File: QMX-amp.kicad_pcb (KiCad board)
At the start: 2 copper layers, 56.6 x 57.7 mm, 4 parts

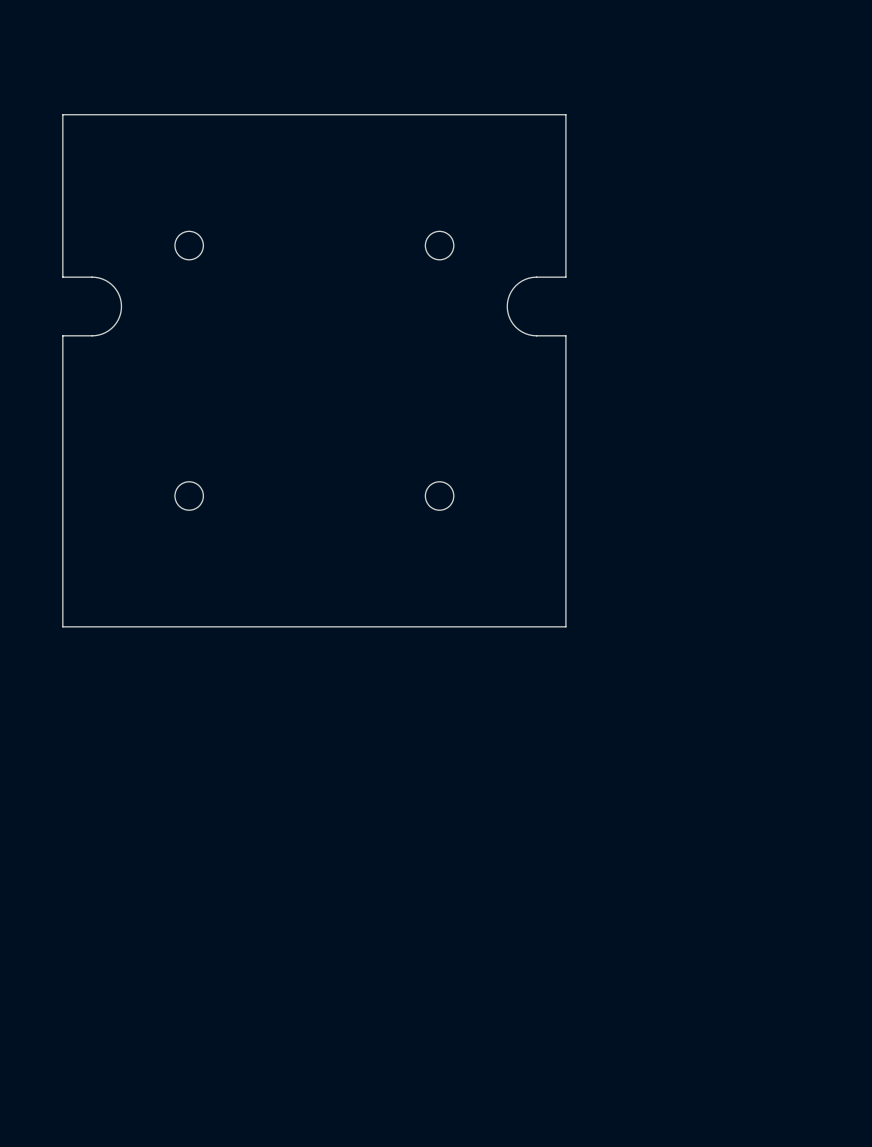
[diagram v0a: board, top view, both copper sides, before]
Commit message: PCB template now fits the QMX dead space
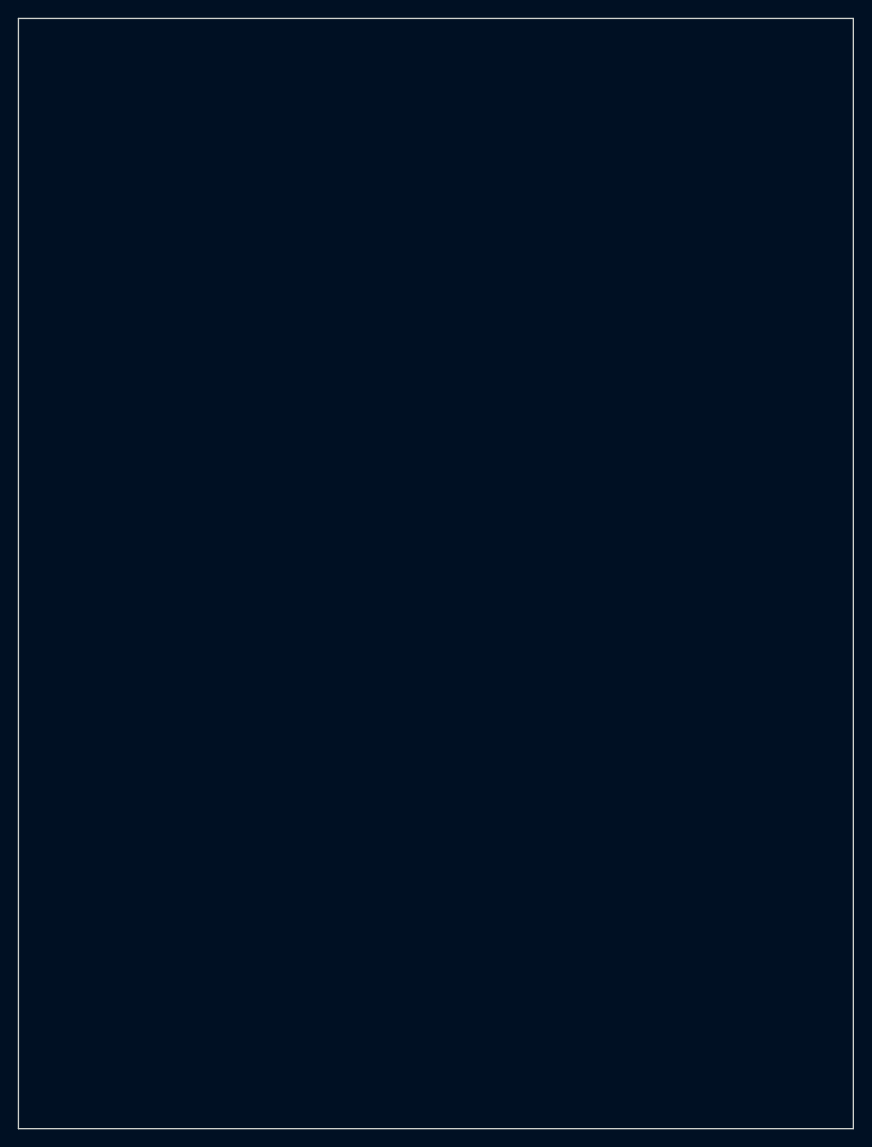
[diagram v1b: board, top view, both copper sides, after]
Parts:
- removed MH1, MH2, MH3, MH4: MountingHole_3.2mm_M3_ISO7380, MountingHole:MountingHole_3.2mm_M3_ISO7380
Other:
- board size 56.6 x 57.7 mm -> 94 x 125 mm

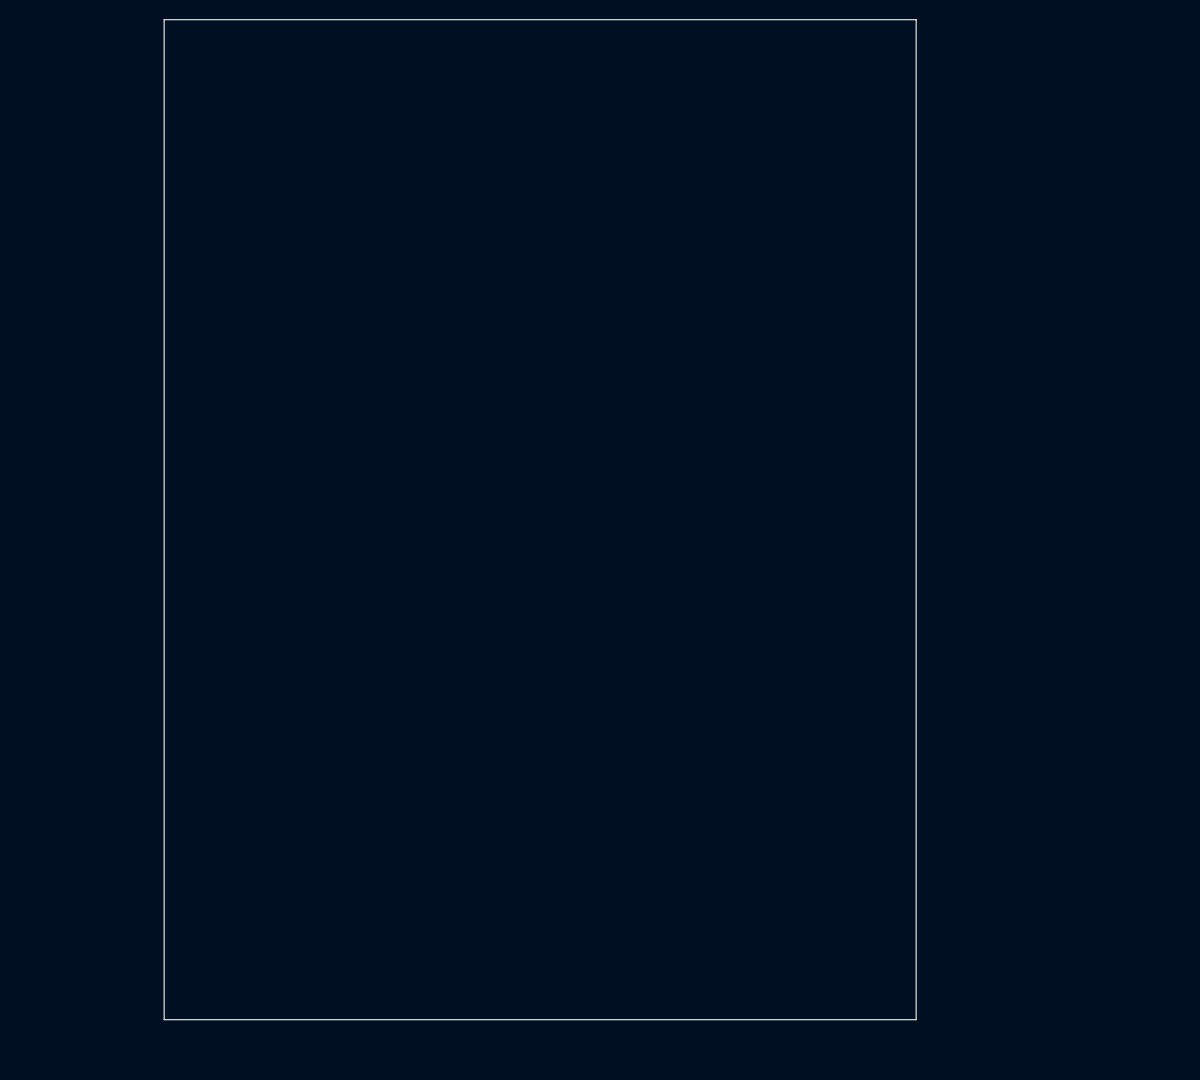
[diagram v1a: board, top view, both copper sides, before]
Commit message: v0.9 ERC passes.  All parts have footprints.  Need to renumber pages so things related are closer in printout
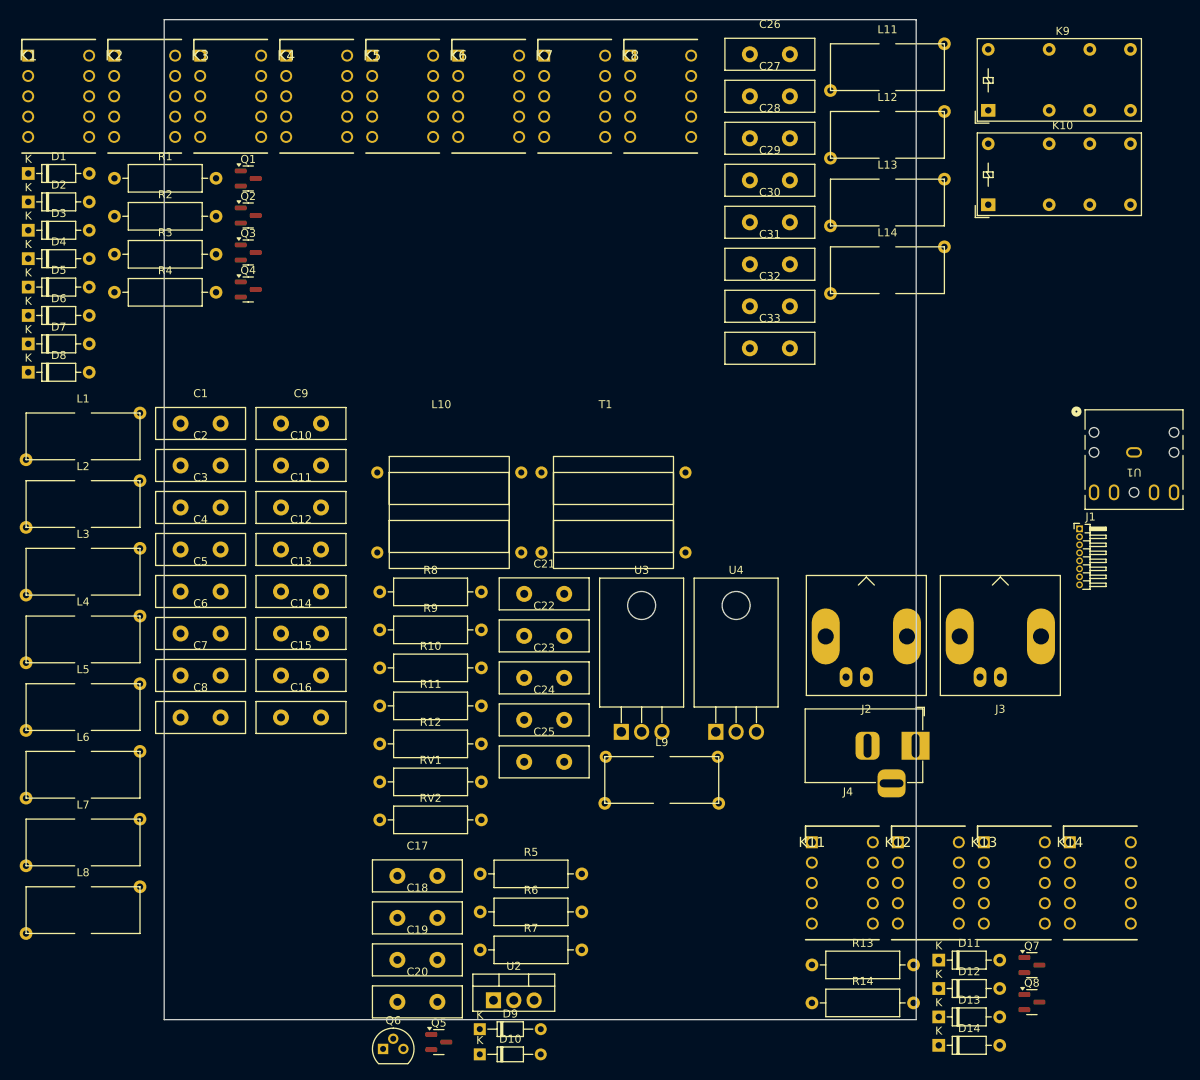
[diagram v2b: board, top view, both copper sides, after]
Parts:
- added C1: 1200 pF, ZZZMyLibrary:C_Disc_D11.0mm_W4.0mm_P5.00mm, F.Cu at (97.0, 82.0)
- added C10: 100 pF, ZZZMyLibrary:C_Disc_D11.0mm_W4.0mm_P5.00mm, F.Cu at (109.6, 87.2)
- added C11: 47 pF, ZZZMyLibrary:C_Disc_D11.0mm_W4.0mm_P5.00mm, F.Cu at (109.6, 92.5)
- added C12: 36 pF, ZZZMyLibrary:C_Disc_D11.0mm_W4.0mm_P5.00mm, F.Cu at (109.6, 97.7)
- added C13: 820 pF, ZZZMyLibrary:C_Disc_D11.0mm_W4.0mm_P5.00mm, F.Cu at (109.6, 103.0)
- added C14: 660 pF, ZZZMyLibrary:C_Disc_D11.0mm_W4.0mm_P5.00mm, F.Cu at (109.6, 108.2)
- added C15: 360 pF, ZZZMyLibrary:C_Disc_D11.0mm_W4.0mm_P5.00mm, F.Cu at (109.6, 113.5)
- added C16: 180 pF, ZZZMyLibrary:C_Disc_D11.0mm_W4.0mm_P5.00mm, F.Cu at (109.6, 118.7)
- added C17: ? uF, ZZZMyLibrary:C_Disc_D11.0mm_W4.0mm_P5.00mm, F.Cu at (124.2, 138.5)
- added C18: 0.1 uF, ZZZMyLibrary:C_Disc_D11.0mm_W4.0mm_P5.00mm, F.Cu at (124.2, 143.8)
- added C19: 0.1 uF, ZZZMyLibrary:C_Disc_D11.0mm_W4.0mm_P5.00mm, F.Cu at (124.2, 149.0)
- added C2: 660 pF, ZZZMyLibrary:C_Disc_D11.0mm_W4.0mm_P5.00mm, F.Cu at (97.0, 87.2)
- added C20: 0.1 uF, ZZZMyLibrary:C_Disc_D11.0mm_W4.0mm_P5.00mm, F.Cu at (124.2, 154.3)
- added C21: 0.1, ZZZMyLibrary:C_Disc_D11.0mm_W4.0mm_P5.00mm, F.Cu at (140.0, 103.3)
- added C22: 0.01, ZZZMyLibrary:C_Disc_D11.0mm_W4.0mm_P5.00mm, F.Cu at (140.0, 108.5)
- added C23: 0.01, ZZZMyLibrary:C_Disc_D11.0mm_W4.0mm_P5.00mm, F.Cu at (140.0, 113.8)
- added C24: 0.1, ZZZMyLibrary:C_Disc_D11.0mm_W4.0mm_P5.00mm, F.Cu at (140.0, 119.0)
- added C25: 1 uF, ZZZMyLibrary:C_Disc_D11.0mm_W4.0mm_P5.00mm, F.Cu at (140.0, 124.3)
- added C26: 120 pF, ZZZMyLibrary:C_Disc_D11.0mm_W4.0mm_P5.00mm, F.Cu at (168.2, 35.8)
- added C27: 68 pF, ZZZMyLibrary:C_Disc_D11.0mm_W4.0mm_P5.00mm, F.Cu at (168.2, 41.1)
- added C28: 180 pF, ZZZMyLibrary:C_Disc_D11.0mm_W4.0mm_P5.00mm, F.Cu at (168.2, 46.3)
- added C29: 120 pF, ZZZMyLibrary:C_Disc_D11.0mm_W4.0mm_P5.00mm, F.Cu at (168.2, 51.6)
- added C3: 360 pF, ZZZMyLibrary:C_Disc_D11.0mm_W4.0mm_P5.00mm, F.Cu at (97.0, 92.5)
- added C30: 13 pF, ZZZMyLibrary:C_Disc_D11.0mm_W4.0mm_P5.00mm, F.Cu at (168.2, 56.8)
- added C31: 100 pF, ZZZMyLibrary:C_Disc_D11.0mm_W4.0mm_P5.00mm, F.Cu at (168.2, 62.1)
- added C32: 82 pF, ZZZMyLibrary:C_Disc_D11.0mm_W4.0mm_P5.00mm, F.Cu at (168.2, 67.3)
- added C33: 68 pF, ZZZMyLibrary:C_Disc_D11.0mm_W4.0mm_P5.00mm, F.Cu at (168.2, 72.6)
- added C4: 180 pF, ZZZMyLibrary:C_Disc_D11.0mm_W4.0mm_P5.00mm, F.Cu at (97.0, 97.7)
- added C5: 2200 pF, ZZZMyLibrary:C_Disc_D11.0mm_W4.0mm_P5.00mm, F.Cu at (97.0, 103.0)
- added C6: 1240 pF, ZZZMyLibrary:C_Disc_D11.0mm_W4.0mm_P5.00mm, F.Cu at (97.0, 108.2)
- added C7: 650 pF, ZZZMyLibrary:C_Disc_D11.0mm_W4.0mm_P5.00mm, F.Cu at (97.0, 113.5)
- added C8: 330 pF, ZZZMyLibrary:C_Disc_D11.0mm_W4.0mm_P5.00mm, F.Cu at (97.0, 118.7)
- added C9: 220 pF, ZZZMyLibrary:C_Disc_D11.0mm_W4.0mm_P5.00mm, F.Cu at (109.6, 82.0)
- added D1: 1N4148, Diode_THT:D_DO-35_SOD27_P7.62mm_Horizontal, F.Cu at (78.0, 50.7)
- added D10: 1N4148, Diode_THT:D_DO-34_SOD68_P7.62mm_Horizontal, F.Cu at (134.4, 160.8)
- added D11: 1N4148, Diode_THT:D_DO-35_SOD27_P7.62mm_Horizontal, F.Cu at (191.8, 149.1)
- added D12: 1N4148, Diode_THT:D_DO-35_SOD27_P7.62mm_Horizontal, F.Cu at (191.8, 152.6)
- added D13: 1N4148, Diode_THT:D_DO-35_SOD27_P7.62mm_Horizontal, F.Cu at (191.8, 156.2)
- added D14: 1N4148, Diode_THT:D_DO-35_SOD27_P7.62mm_Horizontal, F.Cu at (191.8, 159.7)
- added D2: 1N4148, Diode_THT:D_DO-35_SOD27_P7.62mm_Horizontal, F.Cu at (78.0, 54.3)
- added D3: 1N4148, Diode_THT:D_DO-35_SOD27_P7.62mm_Horizontal, F.Cu at (78.0, 57.8)
- added D4: 1N4148, Diode_THT:D_DO-35_SOD27_P7.62mm_Horizontal, F.Cu at (78.0, 61.4)
- added D5: 1N4148, Diode_THT:D_DO-35_SOD27_P7.62mm_Horizontal, F.Cu at (78.0, 64.9)
- added D6: 1N4148, Diode_THT:D_DO-35_SOD27_P7.62mm_Horizontal, F.Cu at (78.0, 68.5)
- added D7: 1N4148, Diode_THT:D_DO-35_SOD27_P7.62mm_Horizontal, F.Cu at (78.0, 72.0)
- added D8: 1N4148, Diode_THT:D_DO-35_SOD27_P7.62mm_Horizontal, F.Cu at (78.0, 75.6)
- added D9: 1N4148, Diode_THT:D_DO-34_SOD68_P7.62mm_Horizontal, F.Cu at (134.4, 157.7)
- added J1: Conn_01x08_Pin, Connector_PinHeader_1.00mm:PinHeader_1x08_P1.00mm_Horizontal, F.Cu at (209.4, 95.2)
- added J2: RF-IN, Connector_Coaxial:BNC_Amphenol_B6252HB-NPP3G-50_Horizontal, F.Cu at (182.8, 113.7)
- added J3: RF-OUT, Connector_Coaxial:BNC_Amphenol_B6252HB-NPP3G-50_Horizontal, F.Cu at (199.5, 113.7)
- added J4: Barrel_Jack_Switch, Connector_BarrelJack:BarrelJack_Horizontal, F.Cu at (188.9, 122.3)
- added K1: EA2-5NU, ZZZMyLibrary:DIPS762W70P254L1420H540Q10N, F.Cu at (78.0, 36.0)
- added K10: HK19F-DCxxV-SHC, Relay_THT:Relay_DPDT_Finder_30.22, F.Cu at (198.0, 54.6)
- added K11: EA2-5NU, ZZZMyLibrary:DIPS762W70P254L1420H540Q10N, F.Cu at (176.0, 134.3)
- added K12: EA2-5NU, ZZZMyLibrary:DIPS762W70P254L1420H540Q10N, F.Cu at (186.7, 134.3)
- added K13: EA2-5NU, ZZZMyLibrary:DIPS762W70P254L1420H540Q10N, F.Cu at (197.5, 134.3)
- added K14: EA2-5NU, ZZZMyLibrary:DIPS762W70P254L1420H540Q10N, F.Cu at (208.2, 134.3)
- added K2: EA2-5NU, ZZZMyLibrary:DIPS762W70P254L1420H540Q10N, F.Cu at (88.8, 36.0)
- added K3: EA2-5NU, ZZZMyLibrary:DIPS762W70P254L1420H540Q10N, F.Cu at (99.5, 36.0)
- added K4: EA2-5NU, ZZZMyLibrary:DIPS762W70P254L1420H540Q10N, F.Cu at (110.2, 36.0)
- added K5: EA2-5NU, ZZZMyLibrary:DIPS762W70P254L1420H540Q10N, F.Cu at (121.0, 36.0)
- added K6: EA2-5NU, ZZZMyLibrary:DIPS762W70P254L1420H540Q10N, F.Cu at (131.8, 36.0)
- added K7: EA2-5NU, ZZZMyLibrary:DIPS762W70P254L1420H540Q10N, F.Cu at (142.5, 36.0)
- added K8: EA2-5NU, ZZZMyLibrary:DIPS762W70P254L1420H540Q10N, F.Cu at (153.2, 36.0)
- added K9: HK19F-DCxxV-SHC, Relay_THT:Relay_DPDT_Finder_30.22, F.Cu at (198.0, 42.8)
- added L1: L, ZZZMyLibrary:Toroid_T50_Vertical_L14.0mm_W5.6mm, F.Cu at (84.9, 80.9)
- added L10: BN-43-7051, ZZZMyLibrary:BN-43-202-FLAT, F.Cu at (129.6, 80.1)
- added L11: L, ZZZMyLibrary:Toroid_T50_Vertical_L14.0mm_W5.6mm, F.Cu at (185.4, 34.8)
- added L12: L, ZZZMyLibrary:Toroid_T50_Vertical_L14.0mm_W5.6mm, F.Cu at (185.4, 43.2)
- added L13: L, ZZZMyLibrary:Toroid_T50_Vertical_L14.0mm_W5.6mm, F.Cu at (185.4, 51.7)
- added L14: L, ZZZMyLibrary:Toroid_T50_Vertical_L14.0mm_W5.6mm, F.Cu at (185.4, 60.2)
- added L2: L, ZZZMyLibrary:Toroid_T50_Vertical_L14.0mm_W5.6mm, F.Cu at (84.9, 89.4)
- added L3: L, ZZZMyLibrary:Toroid_T50_Vertical_L14.0mm_W5.6mm, F.Cu at (84.9, 97.9)
- added L4: L, ZZZMyLibrary:Toroid_T50_Vertical_L14.0mm_W5.6mm, F.Cu at (84.9, 106.3)
- added L5: L, ZZZMyLibrary:Toroid_T50_Vertical_L14.0mm_W5.6mm, F.Cu at (84.9, 114.8)
- added L6: L, ZZZMyLibrary:Toroid_T50_Vertical_L14.0mm_W5.6mm, F.Cu at (84.9, 123.2)
- added L7: L, ZZZMyLibrary:Toroid_T50_Vertical_L14.0mm_W5.6mm, F.Cu at (84.9, 131.7)
- added L8: L, ZZZMyLibrary:Toroid_T50_Vertical_L14.0mm_W5.6mm, F.Cu at (84.9, 140.2)
- added L9: FT50-43, ZZZMyLibrary:Toroid_T50_Vertical_L14.0mm_W5.6mm_4pins, F.Cu at (157.2, 123.9)
- added Q1: BSS123, Package_TO_SOT_SMD:SOT-23, F.Cu at (105.5, 51.4)
- added Q2: BSS123, Package_TO_SOT_SMD:SOT-23, F.Cu at (105.5, 56.0)
- added Q3: BSS123, Package_TO_SOT_SMD:SOT-23, F.Cu at (105.5, 60.6)
- added Q4: BSS123, Package_TO_SOT_SMD:SOT-23, F.Cu at (105.5, 65.2)
- added Q5: BSS123, Package_TO_SOT_SMD:SOT-23, F.Cu at (129.3, 159.3)
- added Q6: MPS-751, Package_TO_SOT_THT:TO-92, F.Cu at (122.4, 160.2)
- added Q7: BSS123, Package_TO_SOT_SMD:SOT-23, F.Cu at (203.5, 149.7)
- added Q8: BSS123, Package_TO_SOT_SMD:SOT-23, F.Cu at (203.5, 154.3)
- added R1: 47K, Resistor_THT:R_Axial_DIN0309_L9.0mm_D3.2mm_P12.70mm_Horizontal, F.Cu at (88.8, 51.3)
- added R10: 270, Resistor_THT:R_Axial_DIN0309_L9.0mm_D3.2mm_P12.70mm_Horizontal, F.Cu at (122.0, 112.5)
- added R11: 470, Resistor_THT:R_Axial_DIN0309_L9.0mm_D3.2mm_P12.70mm_Horizontal, F.Cu at (122.0, 117.3)
- added R12: 470, Resistor_THT:R_Axial_DIN0309_L9.0mm_D3.2mm_P12.70mm_Horizontal, F.Cu at (122.0, 122.0)
- added R13: 47K, Resistor_THT:R_Axial_DIN0309_L9.0mm_D3.2mm_P12.70mm_Horizontal, F.Cu at (176.0, 149.7)
- added R14: 47K, Resistor_THT:R_Axial_DIN0309_L9.0mm_D3.2mm_P12.70mm_Horizontal, F.Cu at (176.0, 154.4)
- added R2: 47K, Resistor_THT:R_Axial_DIN0309_L9.0mm_D3.2mm_P12.70mm_Horizontal, F.Cu at (88.8, 56.1)
- added R3: 47K, Resistor_THT:R_Axial_DIN0309_L9.0mm_D3.2mm_P12.70mm_Horizontal, F.Cu at (88.8, 60.8)
- added R4: 47K, Resistor_THT:R_Axial_DIN0309_L9.0mm_D3.2mm_P12.70mm_Horizontal, F.Cu at (88.8, 65.6)
- added R5: 47K, Resistor_THT:R_Axial_DIN0309_L9.0mm_D3.2mm_P12.70mm_Horizontal, F.Cu at (134.5, 138.3)
- added R6: 4.7K, Resistor_THT:R_Axial_DIN0309_L9.0mm_D3.2mm_P12.70mm_Horizontal, F.Cu at (134.5, 143.0)
- added R7: 4.7K, Resistor_THT:R_Axial_DIN0309_L9.0mm_D3.2mm_P12.70mm_Horizontal, F.Cu at (134.5, 147.8)
- added R8: 270, Resistor_THT:R_Axial_DIN0309_L9.0mm_D3.2mm_P12.70mm_Horizontal, F.Cu at (122.0, 103.0)
- added R9: 21, Resistor_THT:R_Axial_DIN0309_L9.0mm_D3.2mm_P12.70mm_Horizontal, F.Cu at (122.0, 107.8)
- added RV1: 20K, Resistor_THT:R_Axial_DIN0309_L9.0mm_D3.2mm_P12.70mm_Horizontal, F.Cu at (122.0, 126.8)
- added RV2: 20K, Resistor_THT:R_Axial_DIN0309_L9.0mm_D3.2mm_P12.70mm_Horizontal, F.Cu at (122.0, 131.5)
- added T1: BN-43-202, ZZZMyLibrary:BN-43-202-FLAT, F.Cu at (150.2, 80.1)
- added U1: SJ1-3523N, ZZZMyLibrary:SJ1-3523N_CUD, F.Cu at (211.2, 82.6)
- added U2: LM7805_TO220, Package_TO_SOT_THT:TO-220-3_Vertical, F.Cu at (136.2, 154.1)
- added U3: RD16HHF1, Package_TO_SOT_THT:TO-220F-3_Horizontal_TabDown, F.Cu at (152.1, 120.5)
- added U4: RD16HHF1, Package_TO_SOT_THT:TO-220F-3_Horizontal_TabDown, F.Cu at (163.9, 120.5)

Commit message: checkpoint before I shrink width of capps  so things might fit PCB
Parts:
- RV1, RV2: footprint Resistor_THT:R_Axial_DIN0309_L9.0mm_D3.2mm_P12.70mm_Horizontal -> Potentiometer_THT:Potentiometer_Piher_PT-10-V05_Vertical
- moved U3 161.3 mm to (-8.74, 132.1)
- moved U4 161.3 mm to (3.07, 132.1)
- moved L9 138.9 mm to (20.0, 101.9)
- moved C17 132.5 mm to (-8.33, 139.7)
- moved C18 132.5 mm to (-8.33, 144.9)
- moved C19 132.5 mm to (-8.33, 150.2)
- moved C20 132.5 mm to (-8.33, 155.4)
- moved Q5 132.5 mm to (-3.15, 160.5)
- moved D10 132.5 mm to (1.97, 162.0)
- moved D9 132.5 mm to (1.97, 158.8)
- moved Q6 132.5 mm to (-10.1, 161.3)
- moved R5 132.5 mm to (2.02, 139.4)
- moved R6 132.5 mm to (2.02, 144.2)
- moved R7 132.5 mm to (2.02, 148.9)
- moved U2 132.5 mm to (3.68, 155.2)
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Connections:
- J1 pad 7: unconnected-(J1-Pin_7-Pad7) -> GND
- J1 pad 8: unconnected-(J1-Pin_8-Pad8) -> GND
- U1 pad 10: (no net) -> unconnected-(U1-Pad10)
- U1 pad 11: (no net) -> unconnected-(U1-Pad11)
